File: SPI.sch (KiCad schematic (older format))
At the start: 6 parts, among them U18 74HC165, U25 74AHCT595, U6 74AHC273

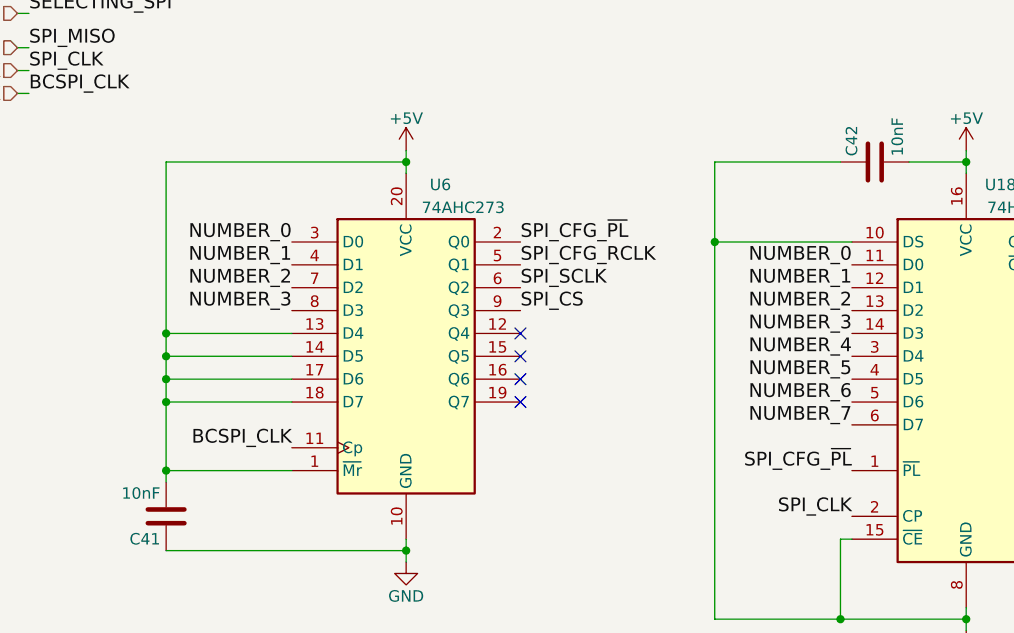
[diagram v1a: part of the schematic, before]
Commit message: Small fix/work-around for SPI
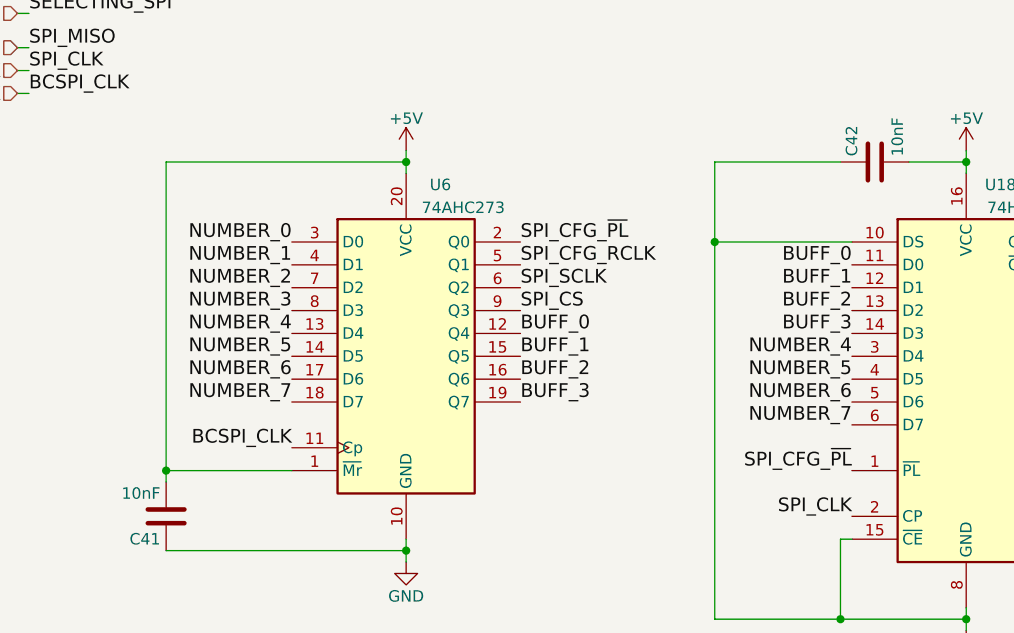
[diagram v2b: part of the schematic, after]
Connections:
- net +5V: no longer U6.13 (D4), U6.14 (D5), U6.17 (D6), U6.18 (D7)
- net NUMBER_0: no longer U18.11 (D0)
- net NUMBER_1: no longer U18.12 (D1)
- net NUMBER_2: no longer U18.13 (D2)
- net NUMBER_3: no longer U18.14 (D3)
- net NUMBER_4: now also U6.13 (D4)
- net NUMBER_5: now also U6.14 (D5)
- net NUMBER_6: now also U6.17 (D6)
- net NUMBER_7: now also U6.18 (D7)
- net BUFF_0: now reaches U6.12 (Q4)
- net BUFF_0: now also U18.11 (D0)
- net BUFF_1: now reaches U6.15 (Q5)
- net BUFF_1: now also U18.12 (D1)
- net BUFF_2: now reaches U6.16 (Q6)
- net BUFF_2: now also U18.13 (D2)
- net BUFF_3: now reaches U6.19 (Q7)
- net BUFF_3: now also U18.14 (D3)
- no-connect marks 6 -> 2
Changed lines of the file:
@@
 Text Label 3650 2600 0    60   ~ 0
 SPI_CS
-Text Label 5100 2400 2    60   ~ 0
-NUMBER_0
-Text Label 5100 2500 2    60   ~ 0
-NUMBER_1
-Text Label 5100 2600 2    60   ~ 0
-NUMBER_2
-Text Label 5100 2700 2    60   ~ 0
-NUMBER_3
 Text Label 5100 2800 2    60   ~ 0
 NUMBER_4
@@
 NoConn ~ 6100 2400
 NoConn ~ 8300 3200
-Wire Wire Line
-	2650 2700 2100 2700
-Connection ~ 2100 2700
-Wire Wire Line
-	2100 2700 2100 1950
-Wire Wire Line
-	2650 2800 2100 2800
-Connection ~ 2100 2800
-Wire Wire Line
-	2100 2800 2100 2700
-Wire Wire Line
-	2650 2900 2100 2900
-Wire Wire Line
-	2100 2800 2100 2900
-Connection ~ 2100 2900
-Wire Wire Line
-	2100 2900 2100 3000
-Wire Wire Line
-	2650 3000 2100 3000
-Connection ~ 2100 3000
-Wire Wire Line
-	2100 3000 2100 3300
-NoConn ~ 3650 3000
-NoConn ~ 3650 2900
-NoConn ~ 3650 2800
-NoConn ~ 3650 2700
 Text HLabel 1450 1450 0    60   Input ~ 0
 SPI_MISO
@@
 Text Label 2650 3200 2    60   ~ 0
 BCSPI_CLK
+Wire Wire Line
+	2100 1950 2100 3300
+Text Label 2650 2700 2    60   ~ 0
+NUMBER_4
+Text Label 2650 2800 2    60   ~ 0
+NUMBER_5
+Text Label 2650 2900 2    60   ~ 0
+NUMBER_6
+Text Label 2650 3000 2    60   ~ 0
+NUMBER_7
+Text Label 3650 2700 0    60   ~ 0
+BUFF_0
+Text Label 3650 2800 0    60   ~ 0
+BUFF_1
+Text Label 3650 2900 0    60   ~ 0
+BUFF_2
+Text Label 3650 3000 0    60   ~ 0
+BUFF_3
+Text Label 5100 2400 2    60   ~ 0
+BUFF_0
+Text Label 5100 2500 2    60   ~ 0
+BUFF_1
+Text Label 5100 2600 2    60   ~ 0
+BUFF_2
+Text Label 5100 2700 2    60   ~ 0
+BUFF_3
 Wire Bus Line
 	1550 4750 1550 5550
